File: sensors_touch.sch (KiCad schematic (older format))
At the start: 21 parts

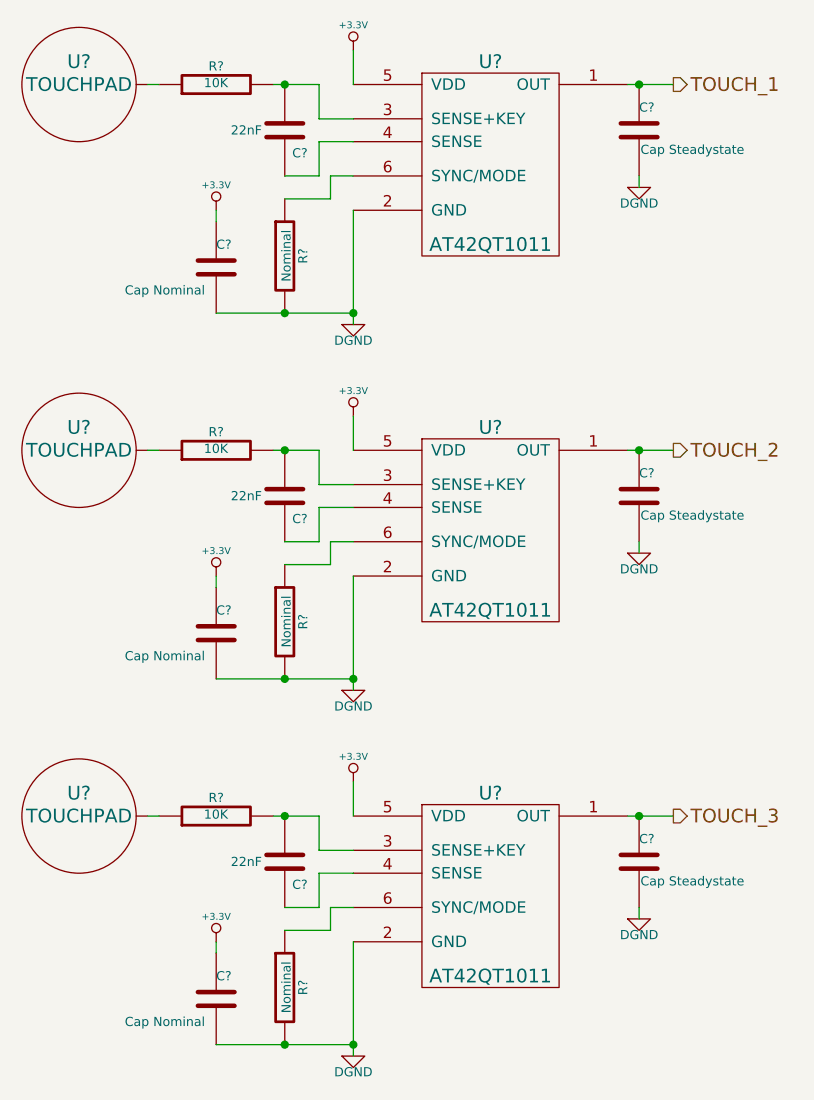
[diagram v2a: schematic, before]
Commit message: various fixes due to issues found in ERC
learned how to use invisible pins
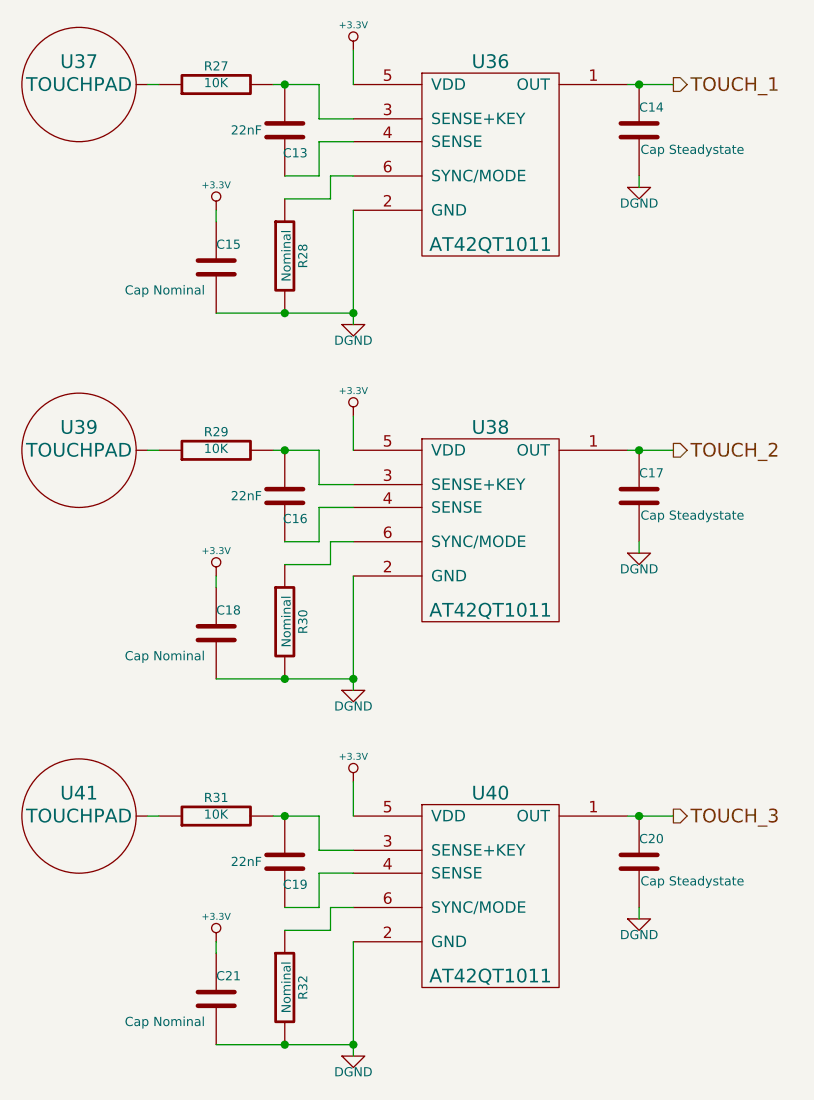
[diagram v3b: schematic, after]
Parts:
- gave numbers to parts that had none: 21
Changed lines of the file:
@@
 Sheet 11 18
 Title ""
-Date "18 dec 2013"
+Date "20 dec 2013"
 Rev ""
 Comp ""
@@
 $EndDescr
 $Comp
-L AT42QT1011 U?
+L AT42QT1011 U36
 U 1 1 527FEAD6
 P 2700 800
-F 0 "U?" H 2700 800 60  0000 C CNN
+F 0 "U36" H 2700 800 60  0000 C CNN
 F 1 "AT42QT1011" H 2700 0   60  0000 C CNN
 F 2 "" H 2700 800 60  0000 C CNN
@@
 $EndComp
 $Comp
-L +3.3V #PWR?
+L +3.3V #PWR054
 U 1 1 527FEAE5
 P 2100 750
-F 0 "#PWR?" H 2100 710 30  0001 C CNN
+F 0 "#PWR054" H 2100 710 30  0001 C CNN
 F 1 "+3.3V" H 2100 860 30  0000 C CNN
 F 2 "" H 2100 750 60  0000 C CNN
@@
 $EndComp
 $Comp
-L DGND #PWR?
+L DGND #PWR055
 U 1 1 527FEB03
 P 2100 1950
-F 0 "#PWR?" H 2100 1950 40  0001 C CNN
+F 0 "#PWR055" H 2100 1950 40  0001 C CNN
 F 1 "DGND" H 2100 1880 40  0000 C CNN
 F 2 "" H 2100 1950 60  0000 C CNN
@@
 $EndComp
 $Comp
-L R R?
+L R R27
 U 1 1 527FEBAE
 P 1500 900
-F 0 "R?" V 1580 900 40  0000 C CNN
+F 0 "R27" V 1580 900 40  0000 C CNN
 F 1 "10K" V 1507 901 40  0000 C CNN
 F 2 "~" V 1430 900 30  0000 C CNN
@@
 $EndComp
 $Comp
-L C C?
+L C C13
 U 1 1 527FEF93
 P 1800 1100
-F 0 "C?" H 1700 1200 40  0000 L CNN
+F 0 "C13" H 1700 1200 40  0000 L CNN
 F 1 "22nF" H 1900 1100 40  0000 L CNN
 F 2 "~" H 1838 950 30  0000 C CNN
@@
 $EndComp
 $Comp
-L TOUCHPAD U?
+L TOUCHPAD U37
 U 1 1 527FF019
 P 900 900
-F 0 "U?" H 900 1000 60  0000 C CNN
+F 0 "U37" H 900 1000 60  0000 C CNN
 F 1 "TOUCHPAD" H 900 900 60  0000 C CNN
 F 2 "" H 900 900 60  0000 C CNN
@@
 	1250 900  1200 900
 Wire Wire Line
-	1750 900  1800 900
-Wire Wire Line
-	1800 900  1950 900
+	1750 900  1950 900
 Wire Wire Line
 	1950 900  1950 1050
@@
 	2100 750  2100 900
 Wire Wire Line
-	2100 1450 2100 1900
-Wire Wire Line
-	2100 1900 2100 1950
+	2100 1450 2100 1950
 Wire Wire Line
 	2000 1400 2000 1300
@@
 	2000 1400 1800 1400
 Wire Wire Line
-	1500 1900 1800 1900
-Wire Wire Line
-	1800 1900 2100 1900
-$Comp
-L C C?
+	1500 1900 2100 1900
+$Comp
+L C C15
 U 1 1 527FF8F3
 P 1500 1700
-F 0 "C?" H 1500 1800 40  0000 L CNN
+F 0 "C15" H 1500 1800 40  0000 L CNN
 F 1 "Cap Nominal" H 1100 1600 40  0000 L CNN
 F 2 "~" H 1538 1550 30  0000 C CNN
@@
 $EndComp
 $Comp
-L +3.3V #PWR?
+L +3.3V #PWR056
 U 1 1 527FFACD
 P 1500 1450
-F 0 "#PWR?" H 1500 1410 30  0001 C CNN
+F 0 "#PWR056" H 1500 1410 30  0001 C CNN
 F 1 "+3.3V" H 1500 1560 30  0000 C CNN
 F 2 "" H 1500 1450 60  0000 C CNN
@@
 Connection ~ 1800 1900
 $Comp
-L C C?
+L C C14
 U 1 1 527FFCCE
 P 3350 1100
-F 0 "C?" H 3350 1200 40  0000 L CNN
+F 0 "C14" H 3350 1200 40  0000 L CNN
 F 1 "Cap Steadystate" H 3356 1015 40  0000 L CNN
 F 2 "~" H 3388 950 30  0000 C CNN
@@
 $EndComp
 Wire Wire Line
-	3300 900  3350 900
-Wire Wire Line
-	3350 900  3500 900
-$Comp
-L DGND #PWR?
+	3300 900  3500 900
+$Comp
+L DGND #PWR057
 U 1 1 527FFCF0
 P 3350 1350
-F 0 "#PWR?" H 3350 1350 40  0001 C CNN
+F 0 "#PWR057" H 3350 1350 40  0001 C CNN
 F 1 "DGND" H 3350 1280 40  0000 C CNN
 F 2 "" H 3350 1350 60  0000 C CNN
@@
 TOUCH_1
 $Comp
-L AT42QT1011 U?
+L AT42QT1011 U38
 U 1 1 528002DB
 P 2700 2400
-F 0 "U?" H 2700 2400 60  0000 C CNN
+F 0 "U38" H 2700 2400 60  0000 C CNN
 F 1 "AT42QT1011" H 2700 1600 60  0000 C CNN
 F 2 "" H 2700 2400 60  0000 C CNN
@@
 $EndComp
 $Comp
-L +3.3V #PWR?
+L +3.3V #PWR058
 U 1 1 528002E1
 P 2100 2350
-F 0 "#PWR?" H 2100 2310 30  0001 C CNN
+F 0 "#PWR058" H 2100 2310 30  0001 C CNN
 F 1 "+3.3V" H 2100 2460 30  0000 C CNN
 F 2 "" H 2100 2350 60  0000 C CNN
@@
 $EndComp
 $Comp
-L DGND #PWR?
+L DGND #PWR059
 U 1 1 528002E7
 P 2100 3550
-F 0 "#PWR?" H 2100 3550 40  0001 C CNN
+F 0 "#PWR059" H 2100 3550 40  0001 C CNN
 F 1 "DGND" H 2100 3480 40  0000 C CNN
 F 2 "" H 2100 3550 60  0000 C CNN
@@
 $EndComp
 $Comp
-L R R?
+L R R29
 U 1 1 528002ED
 P 1500 2500
-F 0 "R?" V 1580 2500 40  0000 C CNN
+F 0 "R29" V 1580 2500 40  0000 C CNN
 F 1 "10K" V 1507 2501 40  0000 C CNN
 F 2 "~" V 1430 2500 30  0000 C CNN
@@
 $EndComp
 $Comp
-L C C?
+L C C16
 U 1 1 528002F3
 P 1800 2700
-F 0 "C?" H 1700 2800 40  0000 L CNN
+F 0 "C16" H 1700 2800 40  0000 L CNN
 F 1 "22nF" H 1900 2700 40  0000 L CNN
 F 2 "~" H 1838 2550 30  0000 C CNN
@@
 $EndComp
 $Comp
-L TOUCHPAD U?
+L TOUCHPAD U39
 U 1 1 528002F9
 P 900 2500
-F 0 "U?" H 900 2600 60  0000 C CNN
+F 0 "U39" H 900 2600 60  0000 C CNN
 F 1 "TOUCHPAD" H 900 2500 60  0000 C CNN
 F 2 "" H 900 2500 60  0000 C CNN
@@
 	1250 2500 1200 2500
 Wire Wire Line
-	1750 2500 1800 2500
-Wire Wire Line
-	1800 2500 1950 2500
+	1750 2500 1950 2500
 Wire Wire Line
 	1950 2500 1950 2650
@@
 	2100 2350 2100 2500
 Wire Wire Line
-	2100 3050 2100 3500
-Wire Wire Line
-	2100 3500 2100 3550
+	2100 3050 2100 3550
 Wire Wire Line
 	2000 3000 2000 2900
@@
 	2000 3000 1800 3000
 Wire Wire Line
-	1500 3500 1800 3500
-Wire Wire Line
-	1800 3500 2100 3500
-$Comp
-L C C?
+	1500 3500 2100 3500
+$Comp
+L C C18
 U 1 1 52800317
 P 1500 3300
-F 0 "C?" H 1500 3400 40  0000 L CNN
+F 0 "C18" H 1500 3400 40  0000 L CNN
 F 1 "Cap Nominal" H 1100 3200 40  0000 L CNN
 F 2 "~" H 1538 3150 30  0000 C CNN
@@
 $EndComp
 $Comp
-L +3.3V #PWR?
+L +3.3V #PWR060
 U 1 1 5280031D
 P 1500 3050
-F 0 "#PWR?" H 1500 3010 30  0001 C CNN
+F 0 "#PWR060" H 1500 3010 30  0001 C CNN
 F 1 "+3.3V" H 1500 3160 30  0000 C CNN
 F 2 "" H 1500 3050 60  0000 C CNN
@@
 Connection ~ 1800 3500
 $Comp
-L C C?
+L C C17
 U 1 1 52800325
 P 3350 2700
-F 0 "C?" H 3350 2800 40  0000 L CNN
+F 0 "C17" H 3350 2800 40  0000 L CNN
 F 1 "Cap Steadystate" H 3356 2615 40  0000 L CNN
 F 2 "~" H 3388 2550 30  0000 C CNN
@@
 $EndComp
 Wire Wire Line
-	3300 2500 3350 2500
-Wire Wire Line
-	3350 2500 3500 2500
-$Comp
-L DGND #PWR?
+	3300 2500 3500 2500
+$Comp
+L DGND #PWR061
 U 1 1 5280032D
 P 3350 2950
-F 0 "#PWR?" H 3350 2950 40  0001 C CNN
+F 0 "#PWR061" H 3350 2950 40  0001 C CNN
 F 1 "DGND" H 3350 2880 40  0000 C CNN
 F 2 "" H 3350 2950 60  0000 C CNN
@@
 TOUCH_2
 $Comp
-L AT42QT1011 U?
+L AT42QT1011 U40
 U 1 1 52800336
 P 2700 4000
-F 0 "U?" H 2700 4000 60  0000 C CNN
+F 0 "U40" H 2700 4000 60  0000 C CNN
 F 1 "AT42QT1011" H 2700 3200 60  0000 C CNN
 F 2 "" H 2700 4000 60  0000 C CNN
@@
 $EndComp
 $Comp
-L +3.3V #PWR?
+L +3.3V #PWR062
 U 1 1 5280033C
 P 2100 3950
-F 0 "#PWR?" H 2100 3910 30  0001 C CNN
+F 0 "#PWR062" H 2100 3910 30  0001 C CNN
 F 1 "+3.3V" H 2100 4060 30  0000 C CNN
 F 2 "" H 2100 3950 60  0000 C CNN
@@
 $EndComp
 $Comp
-L DGND #PWR?
+L DGND #PWR063
 U 1 1 52800342
 P 2100 5150
-F 0 "#PWR?" H 2100 5150 40  0001 C CNN
+F 0 "#PWR063" H 2100 5150 40  0001 C CNN
 F 1 "DGND" H 2100 5080 40  0000 C CNN
 F 2 "" H 2100 5150 60  0000 C CNN
@@
 $EndComp
 $Comp
-L R R?
+L R R31
 U 1 1 52800348
 P 1500 4100
-F 0 "R?" V 1580 4100 40  0000 C CNN
+F 0 "R31" V 1580 4100 40  0000 C CNN
 F 1 "10K" V 1507 4101 40  0000 C CNN
 F 2 "~" V 1430 4100 30  0000 C CNN
@@
 $EndComp
 $Comp
-L C C?
+L C C19
 U 1 1 5280034E
 P 1800 4300
-F 0 "C?" H 1700 4400 40  0000 L CNN
+F 0 "C19" H 1700 4400 40  0000 L CNN
 F 1 "22nF" H 1900 4300 40  0000 L CNN
 F 2 "~" H 1838 4150 30  0000 C CNN
@@
 $EndComp
 $Comp
-L TOUCHPAD U?
+L TOUCHPAD U41
 U 1 1 52800354
 P 900 4100
-F 0 "U?" H 900 4200 60  0000 C CNN
+F 0 "U41" H 900 4200 60  0000 C CNN
 F 1 "TOUCHPAD" H 900 4100 60  0000 C CNN
 F 2 "" H 900 4100 60  0000 C CNN
@@
 	1250 4100 1200 4100
 Wire Wire Line
-	1750 4100 1800 4100
-Wire Wire Line
-	1800 4100 1950 4100
+	1750 4100 1950 4100
 Wire Wire Line
 	1950 4100 1950 4250
@@
 	2100 3950 2100 4100
 Wire Wire Line
-	2100 4650 2100 5100
-Wire Wire Line
-	2100 5100 2100 5150
+	2100 4650 2100 5150
 Wire Wire Line
 	2000 4600 2000 4500
@@
 	2000 4600 1800 4600
 Wire Wire Line
-	1500 5100 1800 5100
-Wire Wire Line
-	1800 5100 2100 5100
-$Comp
-L C C?
+	1500 5100 2100 5100
+$Comp
+L C C21
 U 1 1 52800372
 P 1500 4900
-F 0 "C?" H 1500 5000 40  0000 L CNN
+F 0 "C21" H 1500 5000 40  0000 L CNN
 F 1 "Cap Nominal" H 1100 4800 40  0000 L CNN
 F 2 "~" H 1538 4750 30  0000 C CNN
@@
 $EndComp
 $Comp
-L +3.3V #PWR?
+L +3.3V #PWR064
 U 1 1 52800378
 P 1500 4650
-F 0 "#PWR?" H 1500 4610 30  0001 C CNN
+F 0 "#PWR064" H 1500 4610 30  0001 C CNN
 F 1 "+3.3V" H 1500 4760 30  0000 C CNN
 F 2 "" H 1500 4650 60  0000 C CNN
@@
 Connection ~ 1800 5100
 $Comp
-L C C?
+L C C20
 U 1 1 52800380
 P 3350 4300
-F 0 "C?" H 3350 4400 40  0000 L CNN
+F 0 "C20" H 3350 4400 40  0000 L CNN
 F 1 "Cap Steadystate" H 3356 4215 40  0000 L CNN
 F 2 "~" H 3388 4150 30  0000 C CNN
@@
 $EndComp
 Wire Wire Line
-	3300 4100 3350 4100
-Wire Wire Line
-	3350 4100 3500 4100
-$Comp
-L DGND #PWR?
+	3300 4100 3500 4100
+$Comp
+L DGND #PWR065
 U 1 1 52800388
 P 3350 4550
-F 0 "#PWR?" H 3350 4550 40  0001 C CNN
+F 0 "#PWR065" H 3350 4550 40  0001 C CNN
 F 1 "DGND" H 3350 4480 40  0000 C CNN
 F 2 "" H 3350 4550 60  0000 C CNN
@@
 TOUCH_3
 $Comp
-L R R?
+L R R28
 U 1 1 5280170F
 P 1800 1650
-F 0 "R?" V 1880 1650 40  0000 C CNN
+F 0 "R28" V 1880 1650 40  0000 C CNN
 F 1 "Nominal" V 1807 1651 40  0000 C CNN
 F 2 "~" V 1730 1650 30  0000 C CNN
@@
 $EndComp
 $Comp
-L R R?
+L R R30
 U 1 1 52801715
 P 1800 3250
-F 0 "R?" V 1880 3250 40  0000 C CNN
+F 0 "R30" V 1880 3250 40  0000 C CNN
 F 1 "Nominal" V 1807 3251 40  0000 C CNN
 F 2 "~" V 1730 3250 30  0000 C CNN
@@
 $EndComp
 $Comp
-L R R?
+L R R32
 U 1 1 5280171B
 P 1800 4850
-F 0 "R?" V 1880 4850 40  0000 C CNN
+F 0 "R32" V 1880 4850 40  0000 C CNN
 F 1 "Nominal" V 1807 4851 40  0000 C CNN
 F 2 "~" V 1730 4850 30  0000 C CNN

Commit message: placed components ... quite the task!
there is a lot of shit going on in this board... :D
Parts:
- renumbered C15 to C10, C16 to C11, C17 to C12, C18 to C13, C19 to C14, C20 to C15, C21 to C16, C13 to C8, C14 to C9, R27 to R22, R28 to R23, R29 to R24, R30 to R25, R31 to R26, R32 to R27, U36 to U33, U37 to U34, U38 to U35, U39 to U36, U40 to U37, U41 to U38
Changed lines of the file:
@@
 $Descr A4 11693 8268
 encoding utf-8
-Sheet 11 18
+Sheet 11 15
 Title ""
-Date "12 jan 2014"
+Date "18 jan 2014"
 Rev ""
 Comp ""
@@
 $EndDescr
 $Comp
-L AT42QT1011 U36
+L AT42QT1011 U33
 U 1 1 527FEAD6
 P 2700 800
-F 0 "U36" H 2700 800 60  0000 C CNN
+F 0 "U33" H 2700 800 60  0000 C CNN
 F 1 "AT42QT1011" H 2700 0   60  0000 C CNN
 F 2 "" H 2700 800 60  0000 C CNN
@@
 $EndComp
 $Comp
-L +3.3V #PWR056
+L +3.3V #PWR047
 U 1 1 527FEAE5
 P 2100 750
-F 0 "#PWR056" H 2100 710 30  0001 C CNN
+F 0 "#PWR047" H 2100 710 30  0001 C CNN
 F 1 "+3.3V" H 2100 860 30  0000 C CNN
 F 2 "" H 2100 750 60  0000 C CNN
@@
 $EndComp
 $Comp
-L DGND #PWR057
+L DGND #PWR048
 U 1 1 527FEB03
 P 2100 1950
-F 0 "#PWR057" H 2100 1950 40  0001 C CNN
+F 0 "#PWR048" H 2100 1950 40  0001 C CNN
 F 1 "DGND" H 2100 1880 40  0000 C CNN
 F 2 "" H 2100 1950 60  0000 C CNN
@@
 $EndComp
 $Comp
-L R R27
+L R R22
 U 1 1 527FEBAE
 P 1500 900
-F 0 "R27" V 1580 900 40  0000 C CNN
+F 0 "R22" V 1580 900 40  0000 C CNN
 F 1 "10K" V 1507 901 40  0000 C CNN
 F 2 "~" V 1430 900 30  0000 C CNN
@@
 $EndComp
 $Comp
-L C C13
+L C C8
 U 1 1 527FEF93
 P 1800 1100
-F 0 "C13" H 1700 1200 40  0000 L CNN
+F 0 "C8" H 1700 1200 40  0000 L CNN
 F 1 "22nF" H 1900 1100 40  0000 L CNN
 F 2 "~" H 1838 950 30  0000 C CNN
@@
 $EndComp
 $Comp
-L TOUCHPAD U37
+L TOUCHPAD U34
 U 1 1 527FF019
 P 900 900
-F 0 "U37" H 900 1000 60  0000 C CNN
+F 0 "U34" H 900 1000 60  0000 C CNN
 F 1 "TOUCHPAD" H 900 900 60  0000 C CNN
 F 2 "" H 900 900 60  0000 C CNN
@@
 	1500 1900 2100 1900
 $Comp
-L C C15
+L C C10
 U 1 1 527FF8F3
 P 1500 1700
-F 0 "C15" H 1500 1800 40  0000 L CNN
+F 0 "C10" H 1500 1800 40  0000 L CNN
 F 1 "Cap Nominal" H 1100 1600 40  0000 L CNN
 F 2 "~" H 1538 1550 30  0000 C CNN
@@
 $EndComp
 $Comp
-L +3.3V #PWR058
+L +3.3V #PWR049
 U 1 1 527FFACD
 P 1500 1450
-F 0 "#PWR058" H 1500 1410 30  0001 C CNN
+F 0 "#PWR049" H 1500 1410 30  0001 C CNN
 F 1 "+3.3V" H 1500 1560 30  0000 C CNN
 F 2 "" H 1500 1450 60  0000 C CNN
@@
 Connection ~ 1800 1900
 $Comp
-L C C14
+L C C9
 U 1 1 527FFCCE
 P 3350 1100
-F 0 "C14" H 3350 1200 40  0000 L CNN
+F 0 "C9" H 3350 1200 40  0000 L CNN
 F 1 "Cap Steadystate" H 3356 1015 40  0000 L CNN
 F 2 "~" H 3388 950 30  0000 C CNN
@@
 	3300 900  3500 900
 $Comp
-L DGND #PWR059
+L DGND #PWR050
 U 1 1 527FFCF0
 P 3350 1350
-F 0 "#PWR059" H 3350 1350 40  0001 C CNN
+F 0 "#PWR050" H 3350 1350 40  0001 C CNN
 F 1 "DGND" H 3350 1280 40  0000 C CNN
 F 2 "" H 3350 1350 60  0000 C CNN
@@
 TOUCH_1
 $Comp
-L AT42QT1011 U38
+L AT42QT1011 U35
 U 1 1 528002DB
 P 2700 2400
-F 0 "U38" H 2700 2400 60  0000 C CNN
+F 0 "U35" H 2700 2400 60  0000 C CNN
 F 1 "AT42QT1011" H 2700 1600 60  0000 C CNN
 F 2 "" H 2700 2400 60  0000 C CNN
@@
 $EndComp
 $Comp
-L +3.3V #PWR060
+L +3.3V #PWR051
 U 1 1 528002E1
 P 2100 2350
-F 0 "#PWR060" H 2100 2310 30  0001 C CNN
+F 0 "#PWR051" H 2100 2310 30  0001 C CNN
 F 1 "+3.3V" H 2100 2460 30  0000 C CNN
 F 2 "" H 2100 2350 60  0000 C CNN
@@
 $EndComp
 $Comp
-L DGND #PWR061
+L DGND #PWR052
 U 1 1 528002E7
 P 2100 3550
-F 0 "#PWR061" H 2100 3550 40  0001 C CNN
+F 0 "#PWR052" H 2100 3550 40  0001 C CNN
 F 1 "DGND" H 2100 3480 40  0000 C CNN
 F 2 "" H 2100 3550 60  0000 C CNN
@@
 $EndComp
 $Comp
-L R R29
+L R R24
 U 1 1 528002ED
 P 1500 2500
-F 0 "R29" V 1580 2500 40  0000 C CNN
+F 0 "R24" V 1580 2500 40  0000 C CNN
 F 1 "10K" V 1507 2501 40  0000 C CNN
 F 2 "~" V 1430 2500 30  0000 C CNN
@@
 $EndComp
 $Comp
-L C C16
+L C C11
 U 1 1 528002F3
 P 1800 2700
-F 0 "C16" H 1700 2800 40  0000 L CNN
+F 0 "C11" H 1700 2800 40  0000 L CNN
 F 1 "22nF" H 1900 2700 40  0000 L CNN
 F 2 "~" H 1838 2550 30  0000 C CNN
@@
 $EndComp
 $Comp
-L TOUCHPAD U39
+L TOUCHPAD U36
 U 1 1 528002F9
 P 900 2500
-F 0 "U39" H 900 2600 60  0000 C CNN
+F 0 "U36" H 900 2600 60  0000 C CNN
 F 1 "TOUCHPAD" H 900 2500 60  0000 C CNN
 F 2 "" H 900 2500 60  0000 C CNN
@@
 	1500 3500 2100 3500
 $Comp
-L C C18
+L C C13
 U 1 1 52800317
 P 1500 3300
-F 0 "C18" H 1500 3400 40  0000 L CNN
+F 0 "C13" H 1500 3400 40  0000 L CNN
 F 1 "Cap Nominal" H 1100 3200 40  0000 L CNN
 F 2 "~" H 1538 3150 30  0000 C CNN
@@
 $EndComp
 $Comp
-L +3.3V #PWR062
+L +3.3V #PWR053
 U 1 1 5280031D
 P 1500 3050
-F 0 "#PWR062" H 1500 3010 30  0001 C CNN
+F 0 "#PWR053" H 1500 3010 30  0001 C CNN
 F 1 "+3.3V" H 1500 3160 30  0000 C CNN
 F 2 "" H 1500 3050 60  0000 C CNN
@@
 Connection ~ 1800 3500
 $Comp
-L C C17
+L C C12
 U 1 1 52800325
 P 3350 2700
-F 0 "C17" H 3350 2800 40  0000 L CNN
+F 0 "C12" H 3350 2800 40  0000 L CNN
 F 1 "Cap Steadystate" H 3356 2615 40  0000 L CNN
 F 2 "~" H 3388 2550 30  0000 C CNN
@@
 	3300 2500 3500 2500
 $Comp
-L DGND #PWR063
+L DGND #PWR054
 U 1 1 5280032D
 P 3350 2950
-F 0 "#PWR063" H 3350 2950 40  0001 C CNN
+F 0 "#PWR054" H 3350 2950 40  0001 C CNN
 F 1 "DGND" H 3350 2880 40  0000 C CNN
 F 2 "" H 3350 2950 60  0000 C CNN
@@
 TOUCH_2
 $Comp
-L AT42QT1011 U40
+L AT42QT1011 U37
 U 1 1 52800336
 P 2700 4000
-F 0 "U40" H 2700 4000 60  0000 C CNN
+F 0 "U37" H 2700 4000 60  0000 C CNN
 F 1 "AT42QT1011" H 2700 3200 60  0000 C CNN
 F 2 "" H 2700 4000 60  0000 C CNN
@@
 $EndComp
 $Comp
-L +3.3V #PWR064
+L +3.3V #PWR055
 U 1 1 5280033C
 P 2100 3950
-F 0 "#PWR064" H 2100 3910 30  0001 C CNN
+F 0 "#PWR055" H 2100 3910 30  0001 C CNN
 F 1 "+3.3V" H 2100 4060 30  0000 C CNN
 F 2 "" H 2100 3950 60  0000 C CNN
@@
 $EndComp
 $Comp
-L DGND #PWR065
+L DGND #PWR056
 U 1 1 52800342
 P 2100 5150
-F 0 "#PWR065" H 2100 5150 40  0001 C CNN
+F 0 "#PWR056" H 2100 5150 40  0001 C CNN
 F 1 "DGND" H 2100 5080 40  0000 C CNN
 F 2 "" H 2100 5150 60  0000 C CNN
@@
 $EndComp
 $Comp
-L R R31
+L R R26
 U 1 1 52800348
 P 1500 4100
-F 0 "R31" V 1580 4100 40  0000 C CNN
+F 0 "R26" V 1580 4100 40  0000 C CNN
 F 1 "10K" V 1507 4101 40  0000 C CNN
 F 2 "~" V 1430 4100 30  0000 C CNN
@@
 $EndComp
 $Comp
-L C C19
+L C C14
 U 1 1 5280034E
 P 1800 4300
-F 0 "C19" H 1700 4400 40  0000 L CNN
+F 0 "C14" H 1700 4400 40  0000 L CNN
 F 1 "22nF" H 1900 4300 40  0000 L CNN
 F 2 "~" H 1838 4150 30  0000 C CNN
@@
 $EndComp
 $Comp
-L TOUCHPAD U41
+L TOUCHPAD U38
 U 1 1 52800354
 P 900 4100
-F 0 "U41" H 900 4200 60  0000 C CNN
+F 0 "U38" H 900 4200 60  0000 C CNN
 F 1 "TOUCHPAD" H 900 4100 60  0000 C CNN
 F 2 "" H 900 4100 60  0000 C CNN
@@
 	1500 5100 2100 5100
 $Comp
-L C C21
+L C C16
 U 1 1 52800372
 P 1500 4900
-F 0 "C21" H 1500 5000 40  0000 L CNN
+F 0 "C16" H 1500 5000 40  0000 L CNN
 F 1 "Cap Nominal" H 1100 4800 40  0000 L CNN
 F 2 "~" H 1538 4750 30  0000 C CNN
@@
 $EndComp
 $Comp
-L +3.3V #PWR066
+L +3.3V #PWR057
 U 1 1 52800378
 P 1500 4650
-F 0 "#PWR066" H 1500 4610 30  0001 C CNN
+F 0 "#PWR057" H 1500 4610 30  0001 C CNN
 F 1 "+3.3V" H 1500 4760 30  0000 C CNN
 F 2 "" H 1500 4650 60  0000 C CNN
@@
 Connection ~ 1800 5100
 $Comp
-L C C20
+L C C15
 U 1 1 52800380
 P 3350 4300
-F 0 "C20" H 3350 4400 40  0000 L CNN
+F 0 "C15" H 3350 4400 40  0000 L CNN
 F 1 "Cap Steadystate" H 3356 4215 40  0000 L CNN
 F 2 "~" H 3388 4150 30  0000 C CNN
@@
 	3300 4100 3500 4100
 $Comp
-L DGND #PWR067
+L DGND #PWR058
 U 1 1 52800388
 P 3350 4550
-F 0 "#PWR067" H 3350 4550 40  0001 C CNN
+F 0 "#PWR058" H 3350 4550 40  0001 C CNN
 F 1 "DGND" H 3350 4480 40  0000 C CNN
 F 2 "" H 3350 4550 60  0000 C CNN
@@
 TOUCH_3
 $Comp
-L R R28
+L R R23
 U 1 1 5280170F
 P 1800 1650
-F 0 "R28" V 1880 1650 40  0000 C CNN
+F 0 "R23" V 1880 1650 40  0000 C CNN
 F 1 "Nominal" V 1807 1651 40  0000 C CNN
 F 2 "~" V 1730 1650 30  0000 C CNN
@@
 $EndComp
 $Comp
-L R R30
+L R R25
 U 1 1 52801715
 P 1800 3250
-F 0 "R30" V 1880 3250 40  0000 C CNN
+F 0 "R25" V 1880 3250 40  0000 C CNN
 F 1 "Nominal" V 1807 3251 40  0000 C CNN
 F 2 "~" V 1730 3250 30  0000 C CNN
@@
 $EndComp
 $Comp
-L R R32
+L R R27
 U 1 1 5280171B
 P 1800 4850
-F 0 "R32" V 1880 4850 40  0000 C CNN
+F 0 "R27" V 1880 4850 40  0000 C CNN
 F 1 "Nominal" V 1807 4851 40  0000 C CNN
 F 2 "~" V 1730 4850 30  0000 C CNN
